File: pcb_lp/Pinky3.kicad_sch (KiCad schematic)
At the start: 58 parts, among them J1 MJ-4PP-9, P1 i2c-pin, P2 i2c-pin, SW1 RESET_SW, SW10 SW_PUSH, SW11 SW_PUSH, SW12 SW_PUSH, SW13 SW_PUSH, SW14 SW_PUSH, SW15 SW_PUSH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

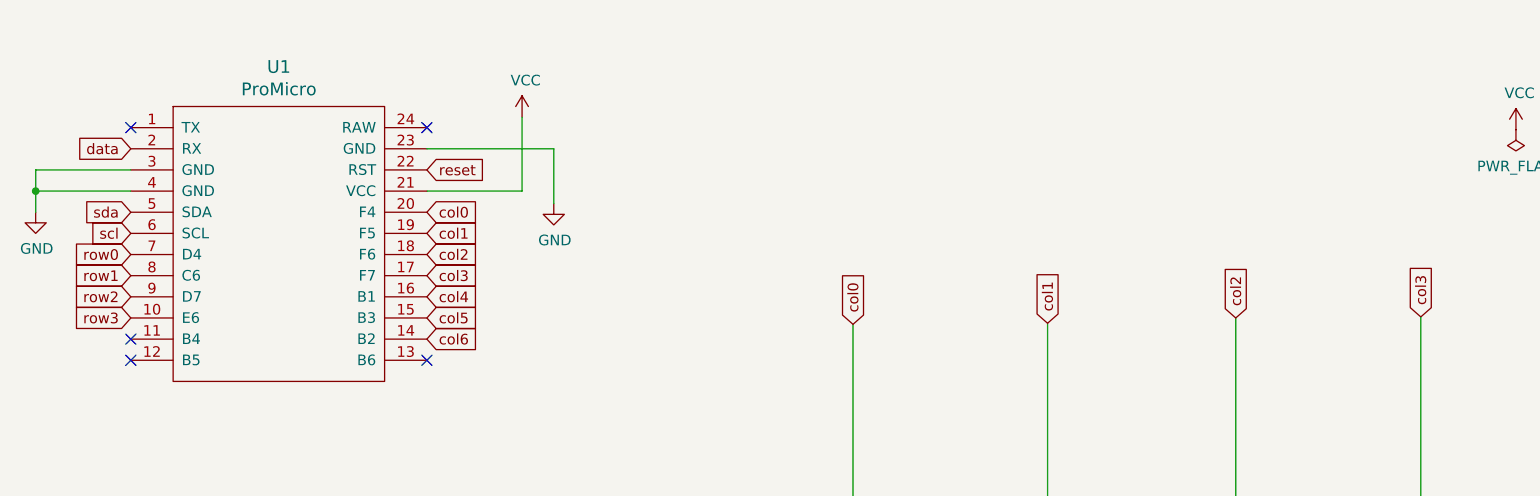
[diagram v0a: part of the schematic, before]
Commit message: update lp version for pcb, switchplate, bottom-plate
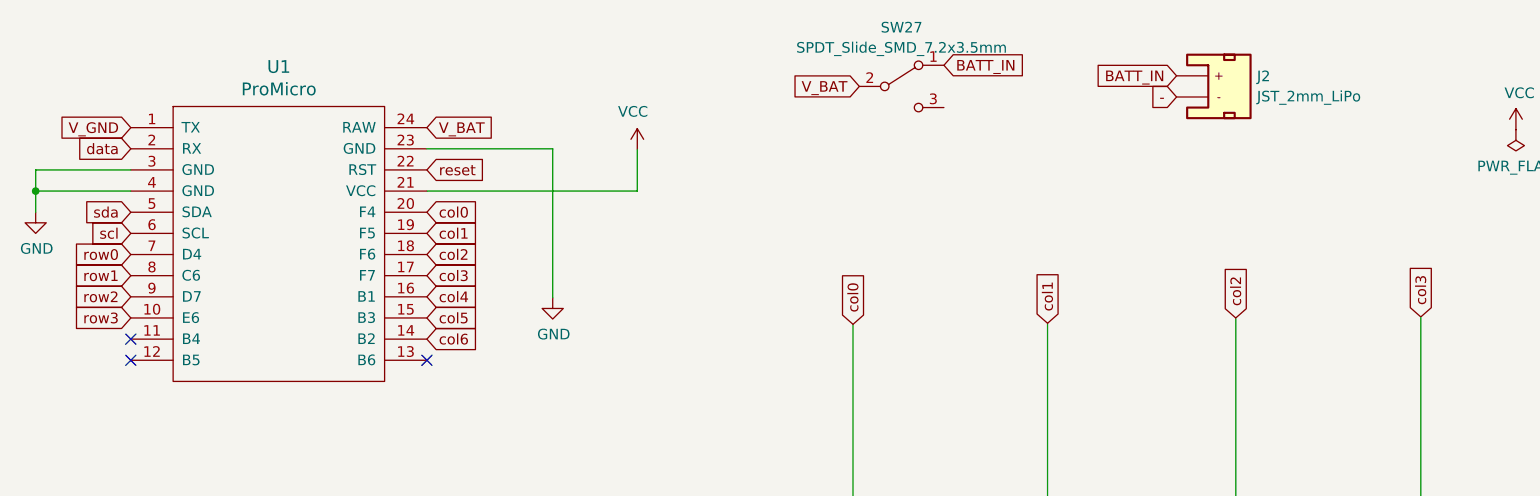
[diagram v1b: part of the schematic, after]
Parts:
- added J2: JST_2mm_LiPo, SparkFun-Connector:JST_SMD_2.0mm-2, symbol PCM_SparkFun-Connector:Conn_01x02_JST_2mm_LiPo
- added SW27: SPDT_Slide_SMD_7.2x3.5mm, SparkFun-Switch:Slide_DPDT_SMD_7.2x3.5mm, symbol SparkFun-Switch:SPDT_Slide_SMD_7.2x3.5mm
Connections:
- net V_GND: now reaches U1.1 (TX)
- net V_BAT: now reaches U1.24 (RAW)
- net V_BAT: now also SW27.2 (B)
- new net: J2.NC1, J2.NC2
- new net -: J2.1 (-)
- new net BATT_IN: J2.2 (+), SW27.1 (A)
- no-connect marks 5 -> 3
